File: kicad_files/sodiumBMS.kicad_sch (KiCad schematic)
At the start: 25 parts, among them J1 USB_C_Receptacle_PowerOnly_6P, U1 STM32F446RETx, U2 INA180A4, U3 INA180A4, U4 LM3940

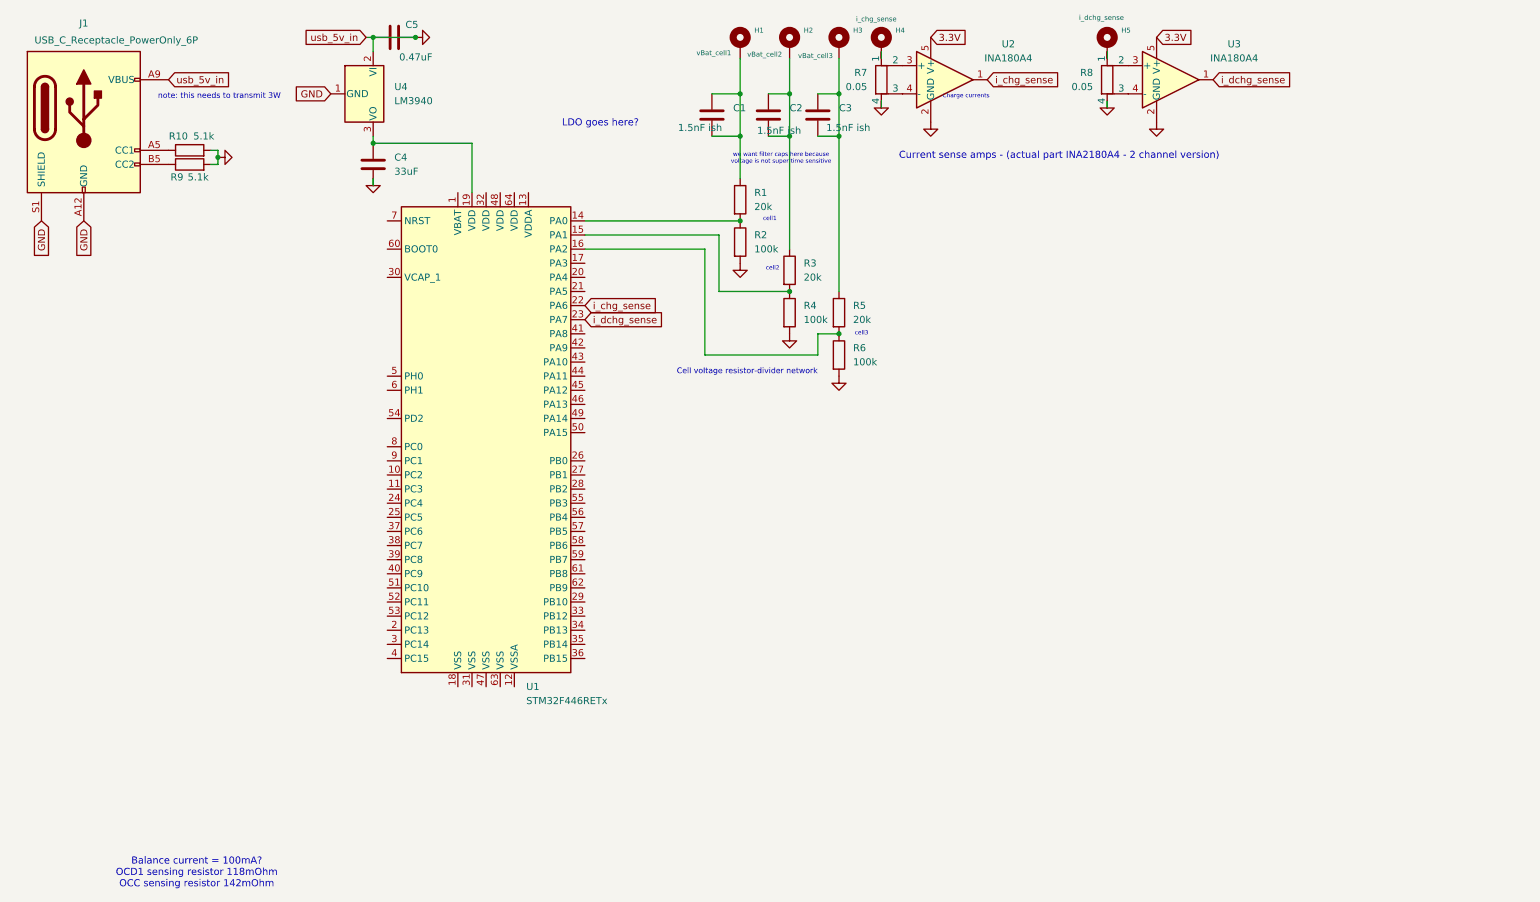
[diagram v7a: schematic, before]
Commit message: begin planning the cell charge path
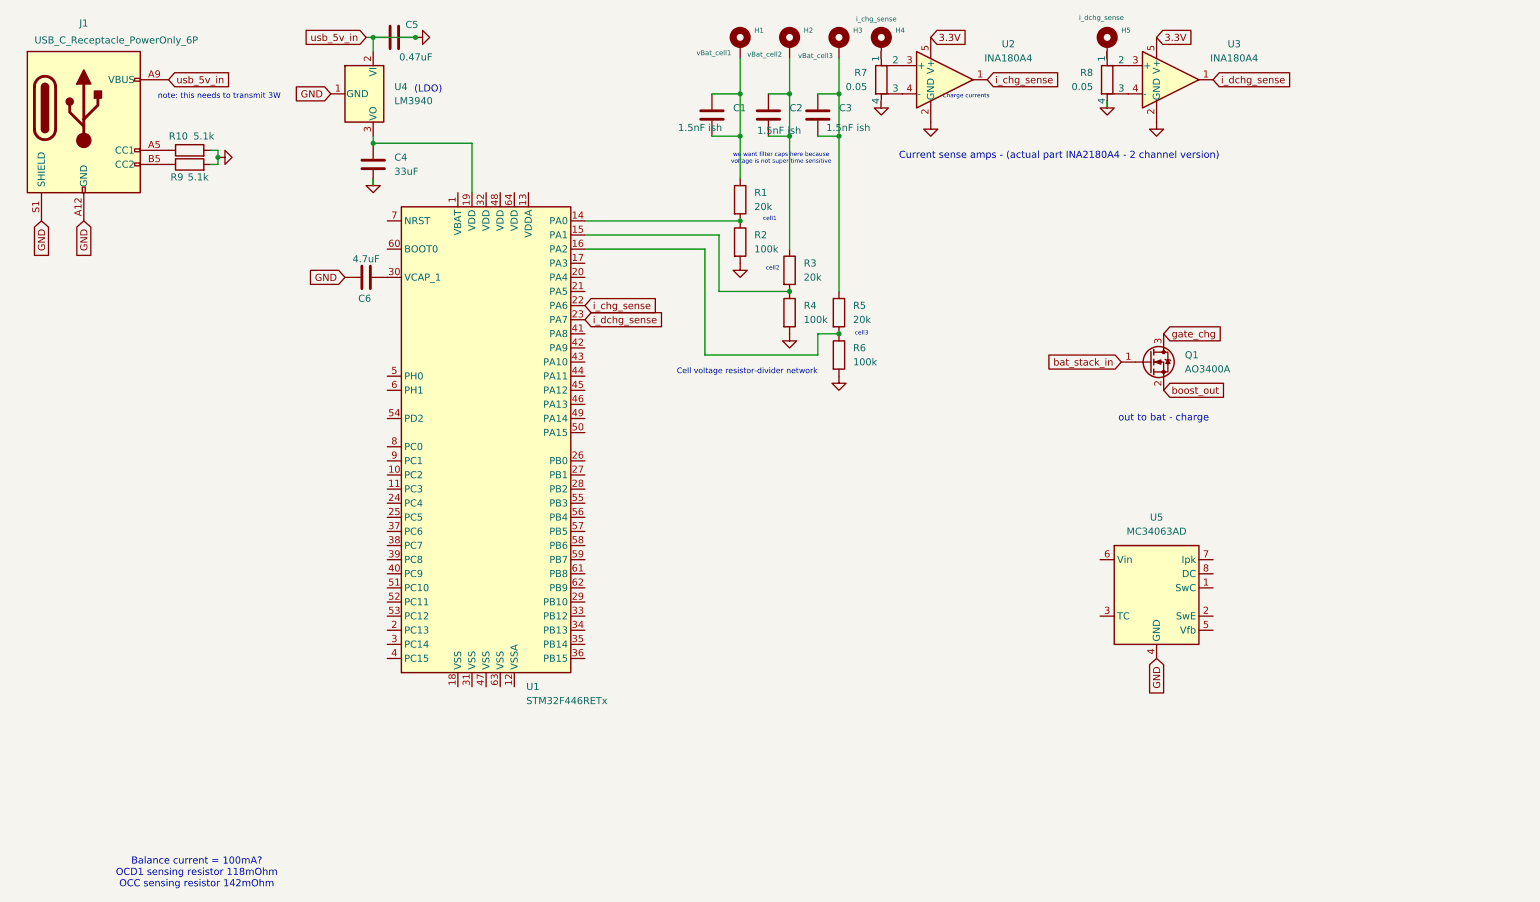
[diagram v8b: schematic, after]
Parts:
- added C6: 4.7uF, symbol Device:C
- added Q1: AO3400A, Package_TO_SOT_SMD:SOT-23, symbol Transistor_FET:AO3400A
- added U5: MC34063AD, Package_SO:SOIC-8_3.9x4.9mm_P1.27mm, symbol Regulator_Switching:MC34063AD
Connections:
- net GND: now also C6.1, U5.4 (GND)
- net at U1.30 (VCAP_1): now also C6.2
- new net bat_stack_in: Q1.1 (G)
- new net boost_out: Q1.2 (S)
- new net gate_chg: Q1.3 (D)
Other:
- note added: "(LDO)"
- note added: "out to bat - charge"
- note removed: "LDO goes here?"
